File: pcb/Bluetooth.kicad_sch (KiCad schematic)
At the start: 15 parts, among them Q6 BC807, U13 RN4870, U14 TXB0102DCU

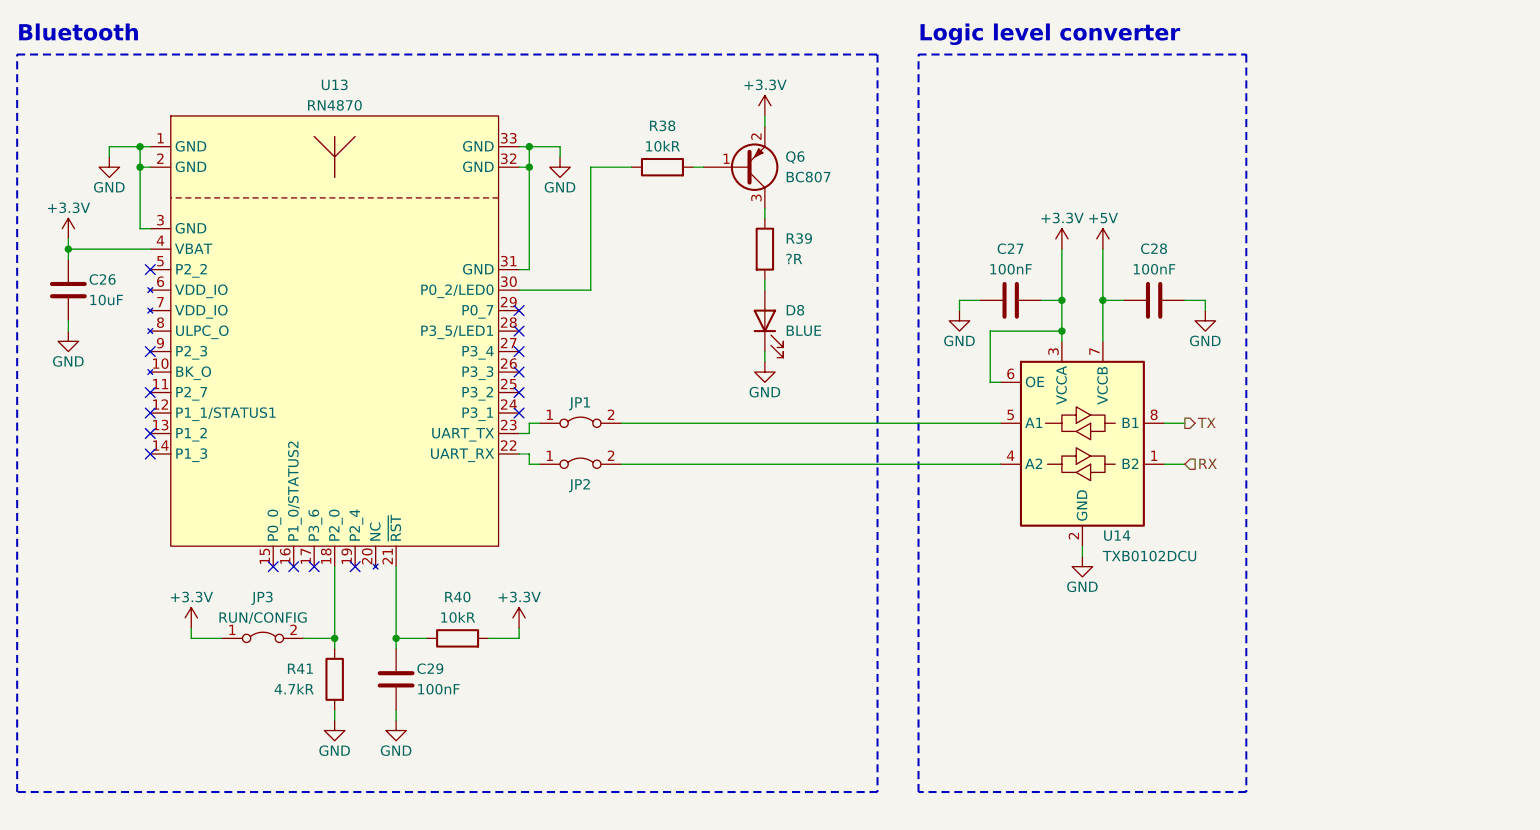
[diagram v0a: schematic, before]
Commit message: Bluetooth RN4870 replaced with RN4678
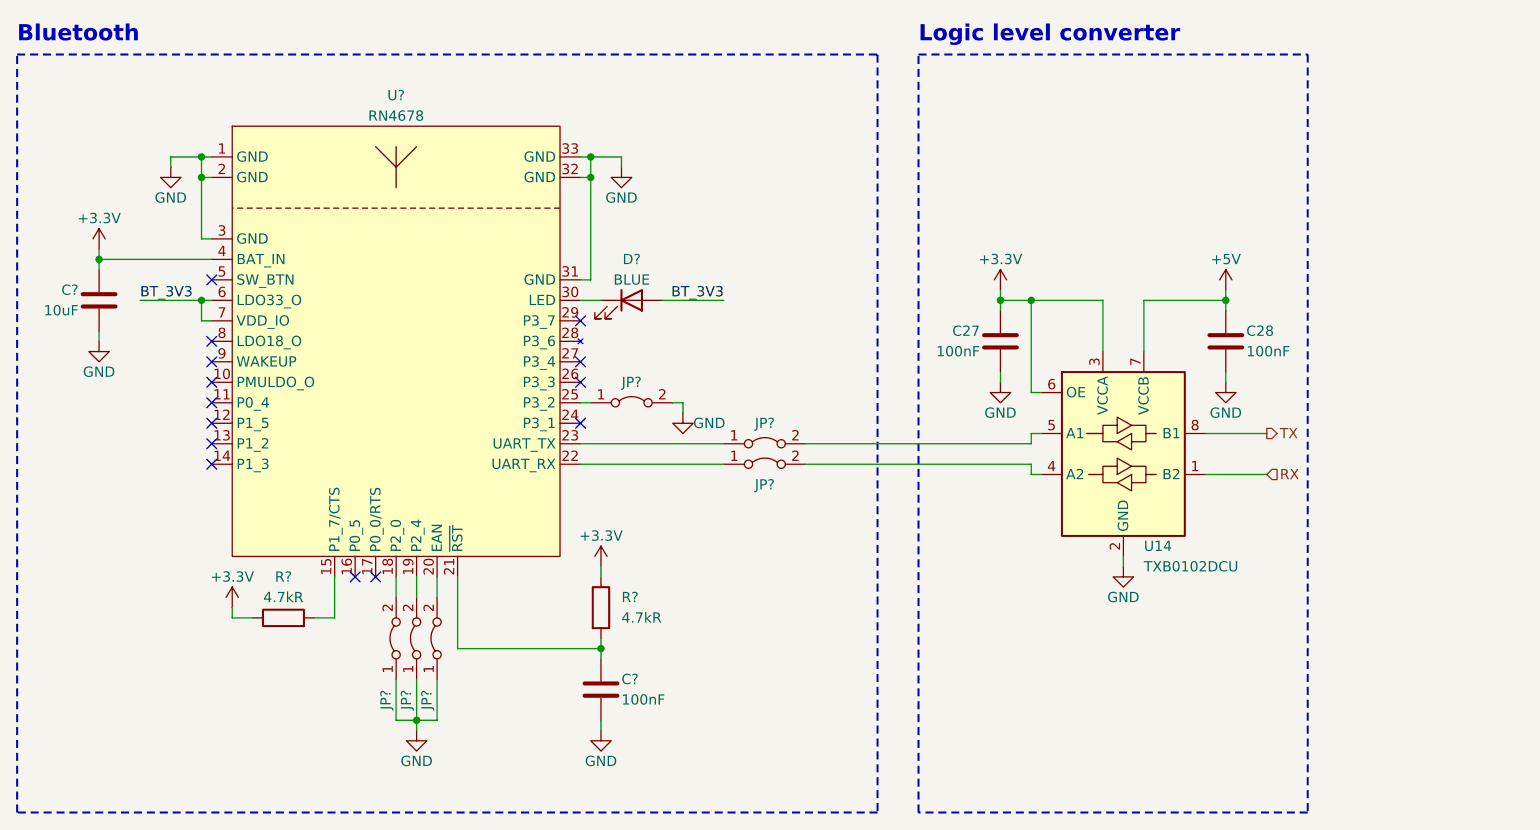
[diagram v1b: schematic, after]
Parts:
- removed C26: 10uF, symbol Device:C
- removed C29: 100nF, symbol Device:C
- removed D8: BLUE, symbol Device:LED
- removed JP1, JP2: Jumper_2_Bridged, symbol Jumper:Jumper_2_Bridged
- removed JP3: RUN/CONFIG, symbol Jumper:Jumper_2_Bridged
- removed Q6: BC807, Package_TO_SOT_SMD:SOT-23, symbol Transistor_BJT:BC807
- removed R38, R40: 10kR, symbol Device:R
- removed R39: ?R, symbol Device:R
- removed R41: 4.7kR, symbol Device:R
- removed U13: RN4870, symbol Autko:RN4870
- added C?: 100nF, symbol Device:C
- added C?: 10uF, symbol Device:C
- added D?: BLUE, symbol Device:LED
- added JP? (x6): Jumper_2_Bridged, symbol Jumper:Jumper_2_Bridged
- added R? (x2): 4.7kR, symbol Device:R
- added U?: RN4678, Autko:RN4678, symbol Autko:RN4678
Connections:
- net +3.3V: now also C?.1, R?.1, R?.1, U?.4 (BAT_IN)
- net GND: now also C?.2, C?.2, JP?.1 (A), JP?.1 (A), JP?.1 (A), JP?.2 (B), U?.1 (GND), U?.2 (GND), U?.3 (GND), U?.31 (GND), U?.32 (GND), U?.33 (GND)
- net at U14.5 (A1): now also JP?.2 (B)
- net at U14.4 (A2): now also JP?.2 (B)
- new net: JP?.1 (A), U?.25 (P3_2)
- new net: R?.2, U?.15 (P1_7/CTS)
- new net: JP?.2 (B), U?.18 (P2_0)
- new net: JP?.2 (B), U?.19 (P2_4)
- new net: JP?.2 (B), U?.20 (EAN)
- new net: C?.1, R?.2, U?.21 (~{RST})
- new net: JP?.1 (A), U?.22 (UART_RX)
- new net: JP?.1 (A), U?.23 (UART_TX)
- new net: D?.1 (K), U?.30 (LED)
- new net BT_3V3: D?.2 (A), U?.6 (LDO33_O), U?.7 (VDD_IO)
- no-connect marks 16 -> 14
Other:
- moved on the sheet: C27, C28, U14

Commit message: Schematic annotated
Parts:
- gave numbers to parts that had none: 12

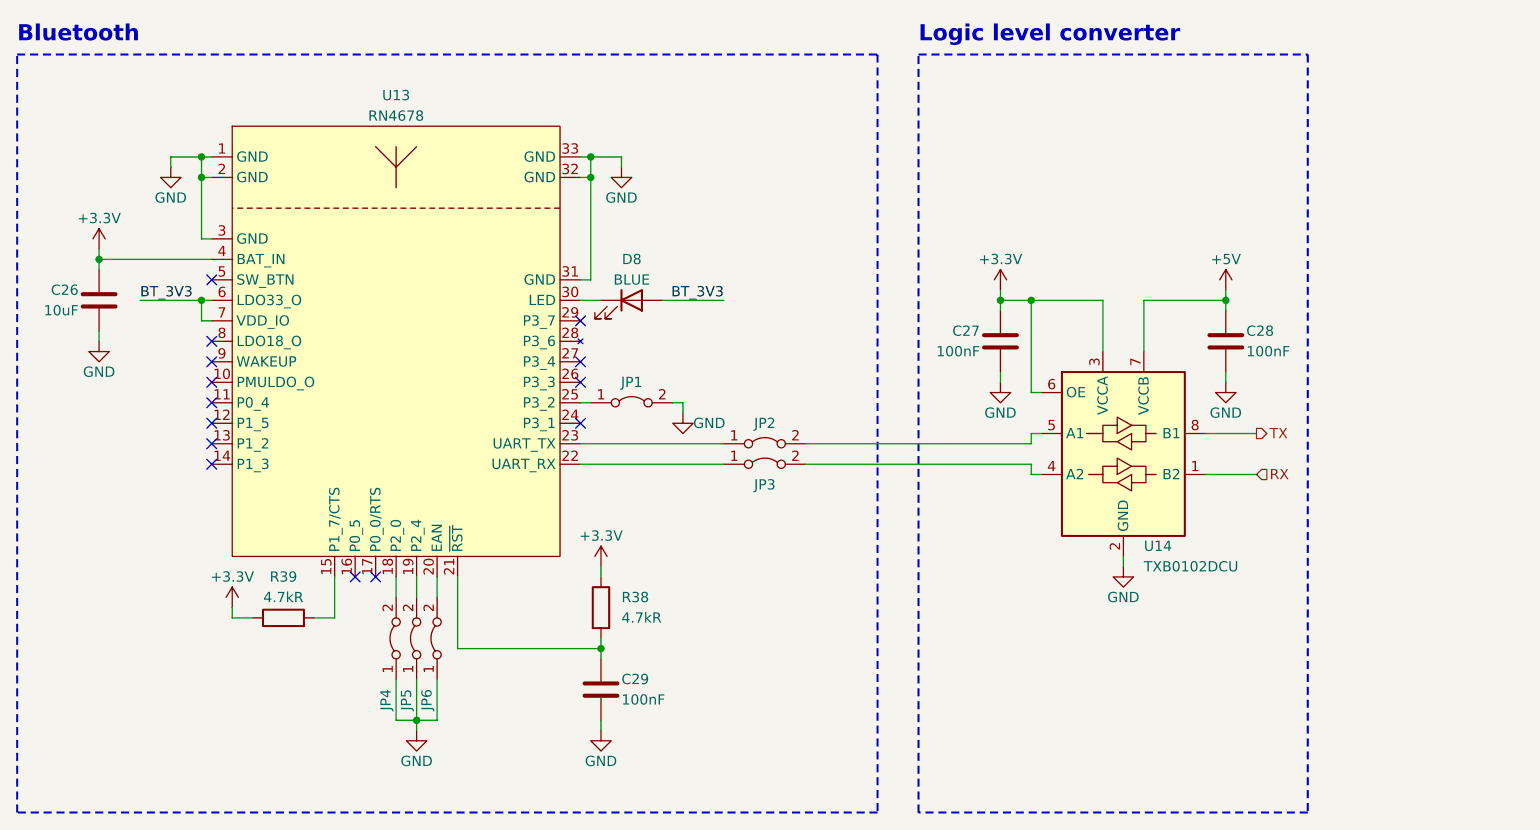
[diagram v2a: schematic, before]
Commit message: [pcb] Test point added
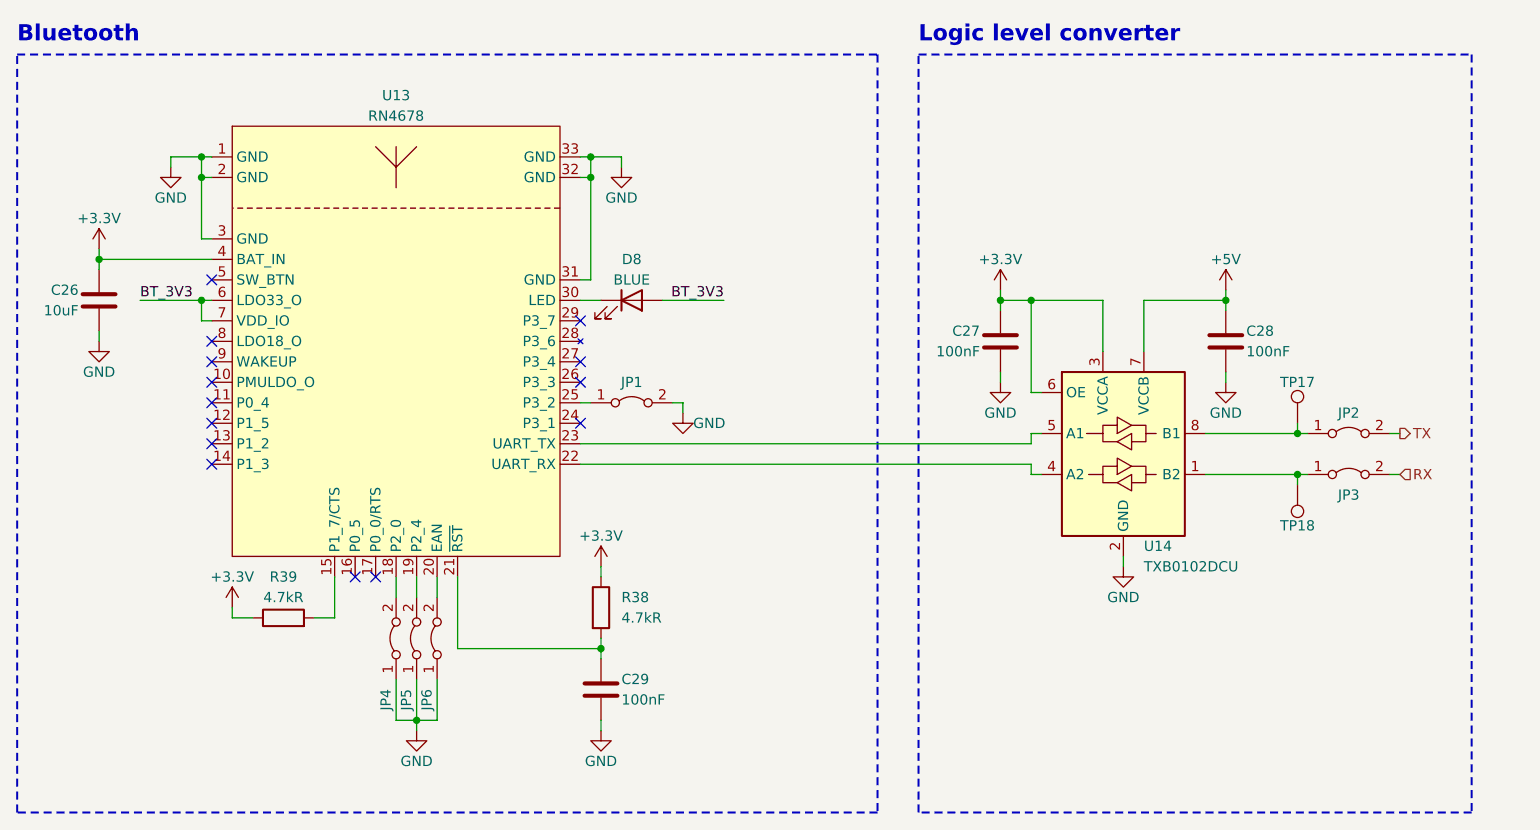
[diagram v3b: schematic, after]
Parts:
- added TP17, TP18: TestPoint, symbol Connector:TestPoint
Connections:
- net RX: now also JP3.2 (B); no longer U14.1 (B2)
- net TX: now also JP2.2 (B); no longer U14.8 (B1)
- net at U13.22 (UART_RX): now also U14.4 (A2); no longer JP3.1 (A)
- net at U13.23 (UART_TX): now also U14.5 (A1); no longer JP2.1 (A)
- new net: JP2.1 (A), TP17.1, U14.8 (B1)
- new net: JP3.1 (A), TP18.1, U14.1 (B2)
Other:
- moved on the sheet: JP2, JP3
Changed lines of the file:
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@@
   (junction (at 143.51 52.07) (diameter 0) (color 0 0 0 0)
   )
+  (junction (at 176.53 73.66) (diameter 0) (color 0 0 0 0)
+  )
   (junction (at 40.64 36.83) (diameter 0) (color 0 0 0 0)
   )
@@
   )
   (junction (at 167.64 52.07) (diameter 0) (color 0 0 0 0)
+  )
+  (junction (at 176.53 68.58) (diameter 0) (color 0 0 0 0)
   )
   (junction (at 67.31 104.14) (diameter 0) (color 0 0 0 0)
@@
     (stroke (width 0) (type default))
   )
+  (wire (pts (xy 165.1 73.66) (xy 176.53 73.66))
+    (stroke (width 0) (type default))
+  )
   (wire (pts (xy 167.64 62.23) (xy 167.64 60.96))
     (stroke (width 0) (type default))
@@
     (stroke (width 0) (type default))
   )
+  (wire (pts (xy 176.53 67.31) (xy 176.53 68.58))
+    (stroke (width 0) (type default))
+  )
   (wire (pts (xy 40.64 44.45) (xy 40.64 36.83))
     (stroke (width 0) (type default))
@@
     (stroke (width 0) (type default))
   )
-  (wire (pts (xy 87.63 69.85) (xy 105.41 69.85))
+  (wire (pts (xy 87.63 69.85) (xy 143.51 69.85))
     (stroke (width 0) (type default))
   )
@@
     (stroke (width 0) (type default))
   )
+  (wire (pts (xy 165.1 68.58) (xy 176.53 68.58))
+    (stroke (width 0) (type default))
+  )
   (wire (pts (xy 152.4 52.07) (xy 152.4 58.42))
     (stroke (width 0) (type default))
   )
+  (wire (pts (xy 187.96 68.58) (xy 189.23 68.58))
+    (stroke (width 0) (type default))
+  )
   (wire (pts (xy 27.94 46.99) (xy 41.91 46.99))
     (stroke (width 0) (type default))
@@
     (stroke (width 0) (type default))
   )
-  (wire (pts (xy 115.57 72.39) (xy 143.51 72.39))
+  (wire (pts (xy 87.63 72.39) (xy 143.51 72.39))
     (stroke (width 0) (type default))
   )
@@
     (stroke (width 0) (type default))
   )
-  (wire (pts (xy 165.1 68.58) (xy 171.45 68.58))
-    (stroke (width 0) (type default))
-  )
   (wire (pts (xy 157.48 52.07) (xy 167.64 52.07))
     (stroke (width 0) (type default))
   )
+  (wire (pts (xy 176.53 73.66) (xy 177.8 73.66))
+    (stroke (width 0) (type default))
+  )
+  (wire (pts (xy 176.53 68.58) (xy 177.8 68.58))
+    (stroke (width 0) (type default))
+  )
   (wire (pts (xy 27.94 45.72) (xy 27.94 46.99))
     (stroke (width 0) (type default))
@@
     (stroke (width 0) (type default))
   )
-  (wire (pts (xy 87.63 72.39) (xy 105.41 72.39))
-    (stroke (width 0) (type default))
-  )
   (wire (pts (xy 87.63 52.07) (xy 90.17 52.07))
     (stroke (width 0) (type default))
   )
+  (wire (pts (xy 176.53 73.66) (xy 176.53 74.93))
+    (stroke (width 0) (type default))
+  )
   (wire (pts (xy 41.91 44.45) (xy 40.64 44.45))
     (stroke (width 0) (type default))
@@
     (stroke (width 0) (type default))
   )
-  (wire (pts (xy 165.1 73.66) (xy 171.45 73.66))
-    (stroke (width 0) (type default))
-  )
   (wire (pts (xy 67.31 104.14) (xy 69.85 104.14))
     (stroke (width 0) (type default))
@@
     (stroke (width 0) (type default))
   )
-  (wire (pts (xy 115.57 69.85) (xy 143.51 69.85))
-    (stroke (width 0) (type default))
-  )
   (wire (pts (xy 67.31 104.14) (xy 67.31 105.41))
     (stroke (width 0) (type default))
@@
   )
   (wire (pts (xy 143.51 73.66) (xy 144.78 73.66))
+    (stroke (width 0) (type default))
+  )
+  (wire (pts (xy 187.96 73.66) (xy 189.23 73.66))
     (stroke (width 0) (type default))
   )
@@
     (fill (type none))
   )
-  (rectangle (start 129.54 21.59) (end 177.8 115.57)
+  (rectangle (start 129.54 21.59) (end 198.12 115.57)
     (stroke (width 0.25) (type dash))
     (fill (type none))
@@
     (effects (font (size 1.27 1.27)) (justify left bottom))
   )
-  (hierarchical_label "RX" (shape input) (at 171.45 73.66 0) (fields_autoplaced)
+  (hierarchical_label "RX" (shape input) (at 189.23 73.66 0) (fields_autoplaced)
     (effects (font (size 1.27 1.27)) (justify left))
   )
-  (hierarchical_label "TX" (shape output) (at 171.45 68.58 0) (fields_autoplaced)
+  (hierarchical_label "TX" (shape output) (at 189.23 68.58 0) (fields_autoplaced)
     (effects (font (size 1.27 1.27)) (justify left))
   )
@@
     )
   )
-  (symbol (lib_id "Jumper:Jumper_2_Bridged") (at 110.49 69.85 0) (unit 1)
-    (in_bom yes) (on_board yes) (dnp no)
-    (property "Reference" "JP2" (at 110.49 67.31 0)
-      (effects (font (size 1.27 1.27)))
-    )
-    (property "Value" "Jumper_2_Bridged" (at 110.49 67.31 0)
-      (effects (font (size 1.27 1.27)) hide)
-    )
-    (property "Footprint" "" (at 110.49 69.85 0)
-      (effects (font (size 1.27 1.27)) hide)
-    )
-    (property "Datasheet" "~" (at 110.49 69.85 0)
+  (symbol (lib_id "Jumper:Jumper_2_Bridged") (at 182.88 68.58 0) (unit 1)
+    (in_bom yes) (on_board yes) (dnp no)
+    (property "Reference" "JP2" (at 182.88 66.04 0)
+      (effects (font (size 1.27 1.27)))
+    )
+    (property "Value" "Jumper_2_Bridged" (at 182.88 66.04 0)
+      (effects (font (size 1.27 1.27)) hide)
+    )
+    (property "Footprint" "" (at 182.88 68.58 0)
+      (effects (font (size 1.27 1.27)) hide)
+    )
+    (property "Datasheet" "~" (at 182.88 68.58 0)
       (effects (font (size 1.27 1.27)) hide)
     )
@@
     )
   )
+  (symbol (lib_id "Connector:TestPoint") (at 176.53 67.31 0) (unit 1)
+    (in_bom yes) (on_board yes) (dnp no)
+    (property "Reference" "TP17" (at 176.53 62.23 0)
+      (effects (font (size 1.27 1.27)))
+    )
+    (property "Value" "TestPoint" (at 179.07 65.913 0)
+      (effects (font (size 1.27 1.27)) (justify left) hide)
+    )
+    (property "Footprint" "" (at 181.61 67.31 0)
+      (effects (font (size 1.27 1.27)) hide)
+    )
+    (property "Datasheet" "~" (at 181.61 67.31 0)
+      (effects (font (size 1.27 1.27)) hide)
+    )
+    (pin "1")
+    (instances
+      (project "Autko"
+        (path "/8d5cfdec-de34-4148-9100-7125640c46f5/bb9a200c-6921-438f-a82b-708524bb5612"
+          (reference "TP17") (unit 1)
+        )
+      )
+    )
+  )
   (symbol (lib_id "Device:C") (at 167.64 57.15 0) (unit 1)
     (in_bom yes) (on_board yes) (dnp no)
@@
     )
   )
+  (symbol (lib_id "Connector:TestPoint") (at 176.53 74.93 180) (unit 1)
+    (in_bom yes) (on_board yes) (dnp no)
+    (property "Reference" "TP18" (at 176.53 80.01 0)
+      (effects (font (size 1.27 1.27)))
+    )
+    (property "Value" "TestPoint" (at 173.99 76.327 0)
+      (effects (font (size 1.27 1.27)) (justify left) hide)
+    )
+    (property "Footprint" "" (at 171.45 74.93 0)
+      (effects (font (size 1.27 1.27)) hide)
+    )
+    (property "Datasheet" "~" (at 171.45 74.93 0)
+      (effects (font (size 1.27 1.27)) hide)
+    )
+    (pin "1")
+    (instances
+      (project "Autko"
+        (path "/8d5cfdec-de34-4148-9100-7125640c46f5/bb9a200c-6921-438f-a82b-708524bb5612"
+          (reference "TP18") (unit 1)
+        )
+      )
+    )
+  )
   (symbol (lib_id "Device:R") (at 90.17 90.17 0) (unit 1)
     (in_bom yes) (on_board yes) (dnp no)
@@
     )
   )
-  (symbol (lib_id "Jumper:Jumper_2_Bridged") (at 110.49 72.39 0) (unit 1)
-    (in_bom yes) (on_board yes) (dnp no)
-    (property "Reference" "JP3" (at 110.49 74.93 0)
-      (effects (font (size 1.27 1.27)))
-    )
-    (property "Value" "Jumper_2_Bridged" (at 110.49 69.85 0)
-      (effects (font (size 1.27 1.27)) hide)
-    )
-    (property "Footprint" "" (at 110.49 72.39 0)
-      (effects (font (size 1.27 1.27)) hide)
-    )
-    (property "Datasheet" "~" (at 110.49 72.39 0)
-      (effects (font (size 1.27 1.27)) hide)
-    )
+  (symbol (lib_id "Jumper:Jumper_2_Bridged") (at 182.88 73.66 0) (unit 1)
+    (in_bom yes) (on_board yes) (dnp no)
+    (property "Reference" "JP3" (at 182.88 76.2 0)
+      (effects (font (size 1.27 1.27)))
+    )
+    (property "Value" "Jumper_2_Bridged" (at 182.88 71.12 0)
+      (effects (font (size 1.27 1.27)) hide)
+    )
+    (property "Footprint" "" (at 182.88 73.66 0)
+      (effects (font (size 1.27 1.27)) hide)
+    )
+    (property "Datasheet" "~" (at 182.88 73.66 0)
+      (effects (font (size 1.27 1.27)) hide)
+    )

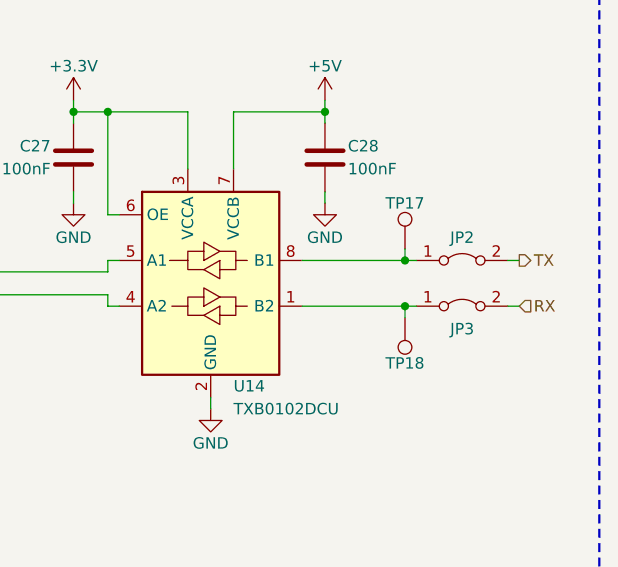
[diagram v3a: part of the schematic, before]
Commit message: [pcb] Schematic clean-up
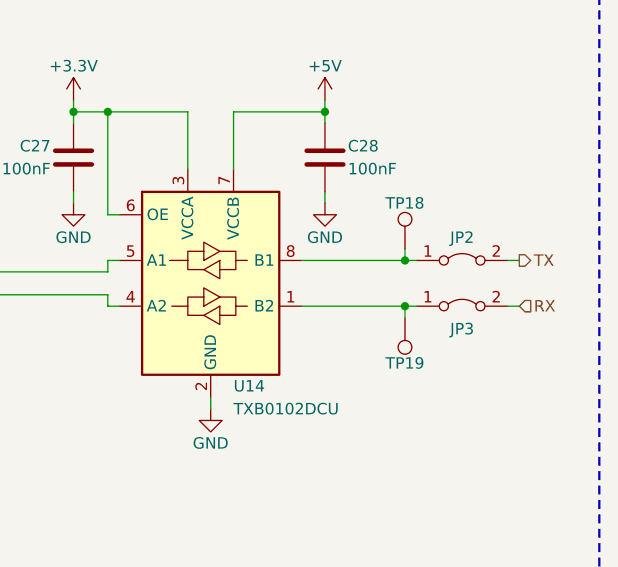
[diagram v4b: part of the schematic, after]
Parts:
- renumbered TP17 to TP18, TP18 to TP19
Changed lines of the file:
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@@
   (symbol (lib_id "Connector:TestPoint") (at 176.53 67.31 0) (unit 1)
     (in_bom yes) (on_board yes) (dnp no)
-    (property "Reference" "TP17" (at 176.53 62.23 0)
+    (property "Reference" "TP18" (at 176.53 62.23 0)
       (effects (font (size 1.27 1.27)))
     )
@@
       (project "Autko"
         (path "/8d5cfdec-de34-4148-9100-7125640c46f5/bb9a200c-6921-438f-a82b-708524bb5612"
-          (reference "TP17") (unit 1)
+          (reference "TP18") (unit 1)
         )
       )
@@
   (symbol (lib_id "Connector:TestPoint") (at 176.53 74.93 180) (unit 1)
     (in_bom yes) (on_board yes) (dnp no)
-    (property "Reference" "TP18" (at 176.53 80.01 0)
+    (property "Reference" "TP19" (at 176.53 80.01 0)
       (effects (font (size 1.27 1.27)))
     )
@@
       (project "Autko"
         (path "/8d5cfdec-de34-4148-9100-7125640c46f5/bb9a200c-6921-438f-a82b-708524bb5612"
-          (reference "TP18") (unit 1)
+          (reference "TP19") (unit 1)
         )
       )
